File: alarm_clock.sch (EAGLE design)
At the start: 31 parts, among them IC1 ATMEGA328P-PU, IC2 MC14489BPE, IC3 DS3231, Q1 16MHz

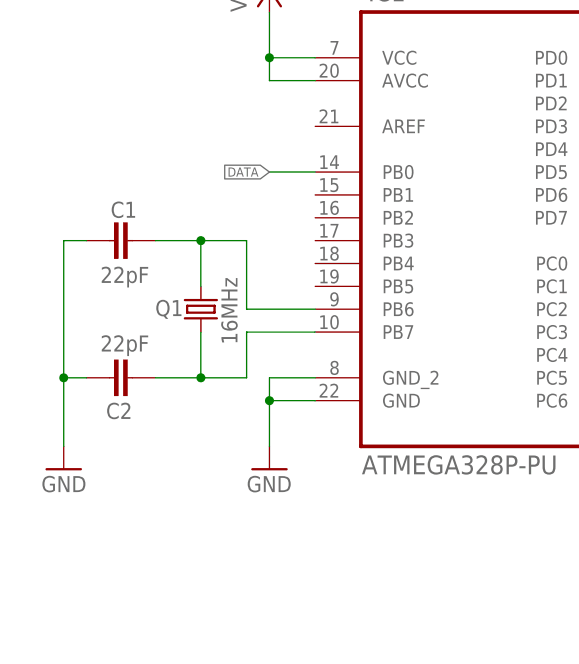
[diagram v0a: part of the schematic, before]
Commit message: crystal oscilator omitted form schematic/board:
internal oscilator of atmega328p to be used ths reducing parts count:
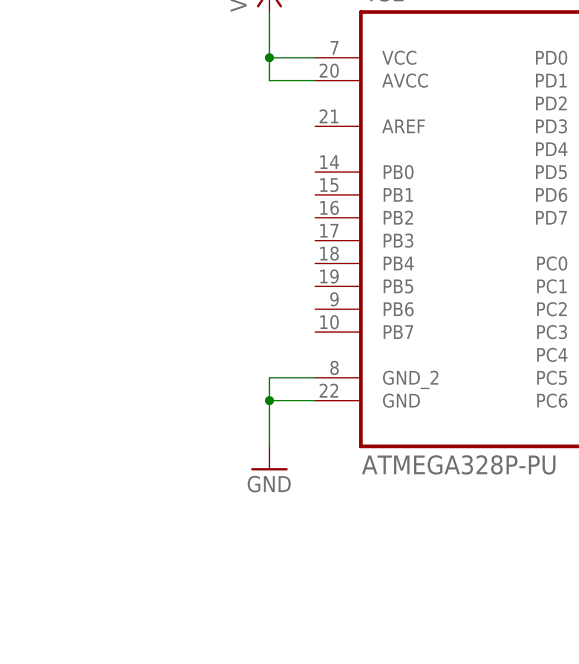
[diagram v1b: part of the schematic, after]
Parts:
- removed C1, C2: 22pF, rcl:C-EU025-024X044
- removed Q1: 16MHz, crystal:CRYSTALHC49S
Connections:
- removed net N$18: C2.2, IC1.PB7, Q1.2
- removed net N$19: C1.2, IC1.PB6, Q1.1
- net DATA: no longer IC1.PB0
- net GND: no longer C1.1, C2.1
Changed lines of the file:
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@@
 <attribute name="MF" value="ATMEL"/>
-</part>
-<part name="Q1" library="crystal" deviceset="CRYSTAL" device="HC49S" value="16MHz">
-<attribute name="MF" value="MULTICOMP"/>
-<attribute name="MPN" value="HC49SM-3.6864-30-50-60-16-ATF"/>
-</part>
-<part name="C1" library="rcl" deviceset="C-EU" device="025-024X044" value="22pF">
-<attribute name="MF" value=""/>
-<attribute name="MPN" value=""/>
-<attribute name="OC_FARNELL" value="unknown"/>
-</part>
-<part name="C2" library="rcl" deviceset="C-EU" device="025-024X044" value="22pF">
-<attribute name="MF" value=""/>
-<attribute name="MPN" value=""/>
-<attribute name="OC_FARNELL" value="unknown"/>
 </part>
 <part name="PIEZO" library="pinhead" deviceset="PINHD-1X2" device="/90">
@@
 <part name="GND3" library="supply1" deviceset="GND" device=""/>
 <part name="GND2" library="supply1" deviceset="GND" device=""/>
-<part name="GND4" library="supply1" deviceset="GND" device=""/>
 <part name="R1" library="pot" deviceset="TRIM_US-" device="CA6V" value="10kΩ">
 <attribute name="MF" value=""/>
@@
 <attribute name="VALUE" x="50.9016" y="192.4812" size="2.0828" layer="96" ratio="10" rot="SR0"/>
 </instance>
-<instance part="Q1" gate="G$1" x="33.02" y="210.82" smashed="yes" rot="MR270">
-<attribute name="NAME" x="27.94" y="211.836" size="1.778" layer="95" rot="MR180"/>
-<attribute name="VALUE" x="37.084" y="214.376" size="1.778" layer="96" rot="MR270"/>
-</instance>
-<instance part="C1" gate="G$1" x="22.86" y="218.44" smashed="yes" rot="MR270">
-<attribute name="OC_FARNELL" x="22.86" y="218.44" size="1.778" layer="96" rot="MR0" display="off"/>
-<attribute name="MF" x="22.86" y="218.44" size="1.778" layer="96" rot="MR0" display="off"/>
-<attribute name="MPN" x="22.86" y="218.44" size="1.778" layer="96" rot="MR0" display="off"/>
-<attribute name="NAME" x="22.987" y="222.758" size="1.778" layer="95" rot="MR180"/>
-<attribute name="VALUE" x="21.844" y="215.519" size="1.778" layer="96" rot="MR180"/>
-</instance>
-<instance part="C2" gate="G$1" x="22.86" y="203.2" smashed="yes" rot="MR270">
-<attribute name="OC_FARNELL" x="22.86" y="203.2" size="1.778" layer="96" rot="MR0" display="off"/>
-<attribute name="MF" x="22.86" y="203.2" size="1.778" layer="96" rot="MR0" display="off"/>
-<attribute name="MPN" x="22.86" y="203.2" size="1.778" layer="96" rot="MR0" display="off"/>
-<attribute name="NAME" x="22.479" y="200.406" size="1.778" layer="95" rot="MR180"/>
-<attribute name="VALUE" x="21.844" y="207.899" size="1.778" layer="96" rot="MR180"/>
-</instance>
 <instance part="PIEZO" gate="G$1" x="231.14" y="116.84" rot="MR0">
 <attribute name="OC_FARNELL" x="231.14" y="116.84" size="1.778" layer="96" rot="MR0" display="off"/>
@@
 <instance part="GND3" gate="1" x="40.64" y="193.04"/>
 <instance part="GND2" gate="1" x="218.44" y="109.22" rot="MR0"/>
-<instance part="GND4" gate="1" x="17.78" y="193.04" rot="MR0"/>
 <instance part="R1" gate="G$1" x="213.36" y="177.8" smashed="yes" rot="MR270">
 <attribute name="OC_FARNELL" x="213.36" y="177.8" size="1.778" layer="96" rot="MR0" display="off"/>
@@
 </segment>
 <segment>
-<pinref part="C2" gate="G$1" pin="1"/>
-<wire x1="20.32" y1="203.2" x2="17.78" y2="203.2" width="0.1524" layer="91"/>
-<pinref part="C1" gate="G$1" pin="1"/>
-<wire x1="17.78" y1="203.2" x2="17.78" y2="218.44" width="0.1524" layer="91"/>
-<wire x1="17.78" y1="218.44" x2="20.32" y2="218.44" width="0.1524" layer="91"/>
-<pinref part="GND4" gate="1" pin="GND"/>
-<wire x1="17.78" y1="195.58" x2="17.78" y2="203.2" width="0.1524" layer="91"/>
-<junction x="17.78" y="203.2"/>
-</segment>
-<segment>
 <pinref part="C5" gate="G$1" pin="2"/>
 <pinref part="GND10" gate="1" pin="GND"/>
@@
 <junction x="218.44" y="124.46"/>
 <pinref part="R8" gate="G$1" pin="E"/>
-</segment>
-</net>
-<net name="N$18" class="0">
-<segment>
-<pinref part="C2" gate="G$1" pin="2"/>
-<pinref part="Q1" gate="G$1" pin="2"/>
-<wire x1="27.94" y1="203.2" x2="33.02" y2="203.2" width="0.1524" layer="91"/>
-<wire x1="33.02" y1="203.2" x2="33.02" y2="208.28" width="0.1524" layer="91"/>
-<wire x1="33.02" y1="203.2" x2="38.1" y2="203.2" width="0.1524" layer="91"/>
-<junction x="33.02" y="203.2"/>
-<wire x1="38.1" y1="203.2" x2="38.1" y2="208.28" width="0.1524" layer="91"/>
-<pinref part="IC1" gate="A" pin="PB7"/>
-<wire x1="38.1" y1="208.28" x2="45.72" y2="208.28" width="0.1524" layer="91"/>
-</segment>
-</net>
-<net name="N$19" class="0">
-<segment>
-<pinref part="C1" gate="G$1" pin="2"/>
-<pinref part="Q1" gate="G$1" pin="1"/>
-<wire x1="27.94" y1="218.44" x2="33.02" y2="218.44" width="0.1524" layer="91"/>
-<wire x1="33.02" y1="218.44" x2="33.02" y2="213.36" width="0.1524" layer="91"/>
-<wire x1="33.02" y1="218.44" x2="38.1" y2="218.44" width="0.1524" layer="91"/>
-<junction x="33.02" y="218.44"/>
-<wire x1="38.1" y1="218.44" x2="38.1" y2="210.82" width="0.1524" layer="91"/>
-<pinref part="IC1" gate="A" pin="PB6"/>
-<wire x1="38.1" y1="210.82" x2="45.72" y2="210.82" width="0.1524" layer="91"/>
 </segment>
 </net>
@@
 <net name="DATA" class="0">
 <segment>
-<pinref part="IC1" gate="A" pin="PB0"/>
-<wire x1="45.72" y1="226.06" x2="40.64" y2="226.06" width="0.1524" layer="91"/>
-<label x="40.64" y="226.06" size="1.016" layer="95" rot="R180" xref="yes"/>
-</segment>
-<segment>
 <pinref part="IC2" gate="A" pin="DATA_IN"/>
